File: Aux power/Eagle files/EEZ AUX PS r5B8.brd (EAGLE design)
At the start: 107 x 74 mm, 78 parts, among them IC1 LM25575, IC2 MC7812, IC3 TPD4E002DRLR, IC4 TPD2E001DZDR, IC5 ADUM3160BRWZ, Q1 BTA26-600, Q2 BTA26-600, Q3 IRLL014N, X1 282836-5, X2 09185067324, X3 22-23-2031, X4 LMJ2138812S0LOT6C, X5 826629-8, X6 826629-5, X7 SSW-105-02-S-S, X8 2411-01

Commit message: Rt value corrections for AUX PS and Power board
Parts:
- R11: value 30K -> 18K
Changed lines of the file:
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@@
 <text x="15.6845" y="37.9476" size="1.016" layer="125" ratio="10" rot="R180">SAR1</text>
 <text x="42.1505125" y="57.57349375" size="2.1844" layer="125" ratio="10" rot="SR0">TR1</text>
-<text x="13.035509375" y="57.16549375" size="1.27" layer="125" ratio="10">VAR1</text>
-<text x="17.861509375" y="57.16549375" size="1.27" layer="125" ratio="10">VAR2</text>
+<text x="12.845009375" y="57.16549375" size="1.27" layer="125" ratio="10">VAR1</text>
+<text x="17.925009375" y="57.16549375" size="1.27" layer="125" ratio="10">VAR2</text>
 <text x="1.613003125" y="61.6315" size="1.27" layer="125" ratio="10">X1</text>
 <text x="103.981503125" y="67.197503125" size="1.27" layer="125" ratio="10">X2</text>
@@
 <attribute name="VALUE" x="82.169" y="28.2575" size="1.016" layer="27" ratio="10"/>
 </element>
-<element name="R11" library="rcl" package="R0805" value="30K" x="82.2325" y="26.7335" smashed="yes">
+<element name="R11" library="rcl" package="R0805" value="18K" x="82.2325" y="26.7335" smashed="yes">
 <attribute name="NAME" x="81.1149" y="24.5364" size="1.016" layer="25" ratio="10"/>
 <attribute name="VALUE" x="84.0486" y="27.1399" size="0.9906" layer="27" ratio="10" rot="R180"/>
@@
 <element name="C8" library="rcl" package="C0805" value="100n" x="79.3115" y="36.957" smashed="yes" rot="R180">
 <attribute name="NAME" x="81.407" y="37.6555" size="1.016" layer="25" ratio="10" rot="SR270"/>
-<attribute name="VALUE" x="81.534" y="37.4015" size="1.27" layer="27" rot="R180"/>
+<attribute name="VALUE" x="77.597" y="36.449" size="1.016" layer="27" ratio="10"/>
 </element>
 <element name="C7" library="rcl" package="C0805" value="22n" x="85.217" y="28.0035" smashed="yes" rot="R270">
@@
 <element name="R7" library="rcl" package="R0805" value="15K" x="71.9455" y="36.83" smashed="yes" rot="R270">
 <attribute name="NAME" x="69.7865" y="37.5285" size="1.016" layer="25" ratio="10" rot="SR270"/>
-<attribute name="VALUE" x="71.3105" y="38.354" size="1.27" layer="27" rot="R270"/>
+<attribute name="VALUE" x="71.374" y="38.227" size="1.016" layer="27" ratio="10" rot="R270"/>
 </element>
 <element name="R8" library="rcl" package="R0805" value="2K2" x="71.9455" y="40.767" smashed="yes" rot="R270">
 <attribute name="NAME" x="71.1835" y="42.926" size="1.016" layer="25" ratio="10"/>
-<attribute name="VALUE" x="72.4535" y="39.1795" size="1.27" layer="27" rot="R90"/>
+<attribute name="VALUE" x="72.4535" y="39.497" size="1.016" layer="27" ratio="10" rot="R90"/>
 </element>
 <element name="C9" library="rcl" package="C1210" value="4u7" x="71.501" y="47.625" smashed="yes" rot="R180">
@@
 <element name="X1" library="EEZ_Lib1" package="TBLOCK5.0_5" value="282836-5" x="4.4625" y="58.155" smashed="yes">
 <attribute name="NAME" x="1.613" y="61.6315" size="1.27" layer="25" ratio="10"/>
-<attribute name="VALUE" x="0.1525" y="33.265" size="1.27" layer="27"/>
+<attribute name="VALUE" x="1.66" y="43.7135" size="1.27" layer="27" rot="R90"/>
 </element>
 <element name="ZD2" library="EEZ_Lib1" package="DO201-BIDIR" value="1.5KE400CA" x="12.5355" y="23.737" smashed="yes">
@@
 <element name="L1" library="EEZ_Lib1" package="L1210" value="2u2" x="72.009" y="32.766" smashed="yes">
 <attribute name="NAME" x="68.2625" y="33.5915" size="1.27" layer="25" ratio="10" rot="SR270"/>
-<attribute name="VALUE" x="71.4375" y="34.417" size="1.27" layer="27" rot="R270"/>
+<attribute name="VALUE" x="70.358" y="32.131" size="1.27" layer="27"/>
 </element>
 <element name="Q1" library="triac" package="TOP3S-1" value="BTA26-600" x="46.0375" y="13.0175" smashed="yes" rot="R180">

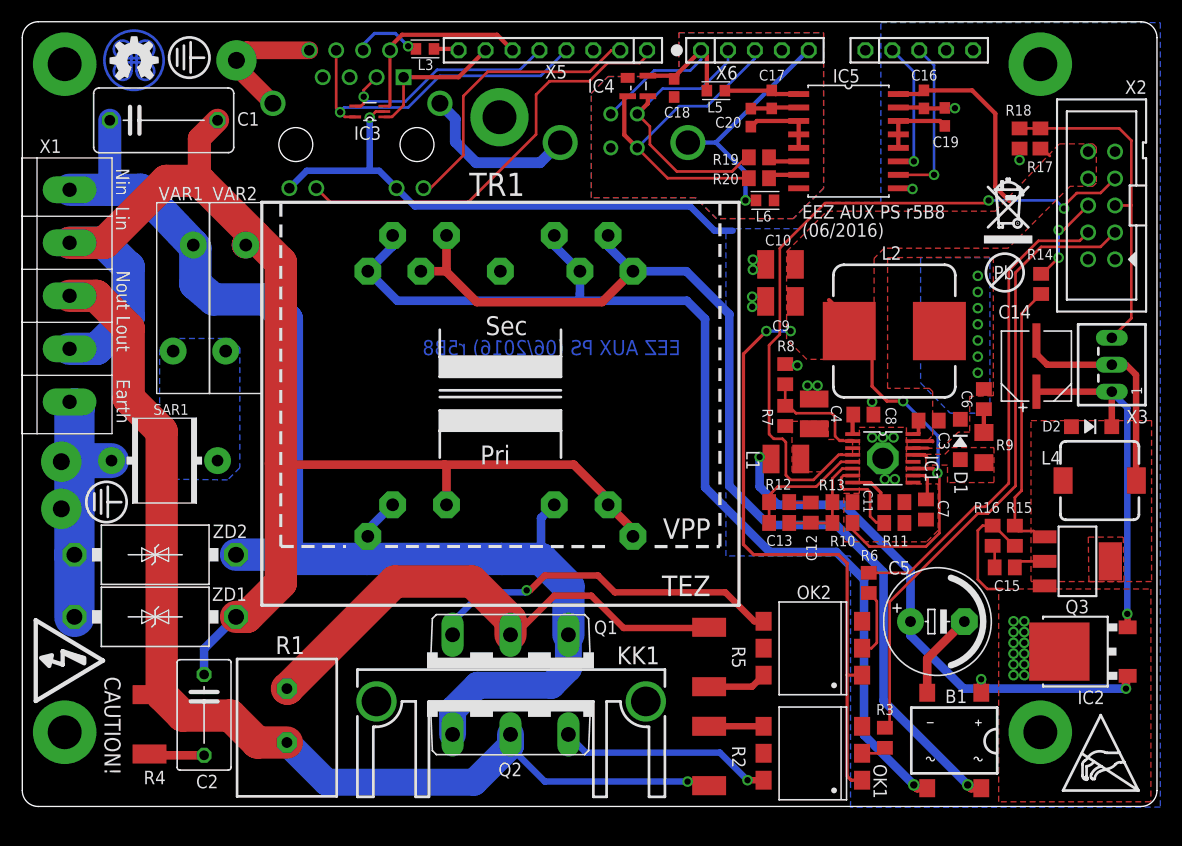
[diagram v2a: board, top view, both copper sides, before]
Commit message: AUX PS renumbering
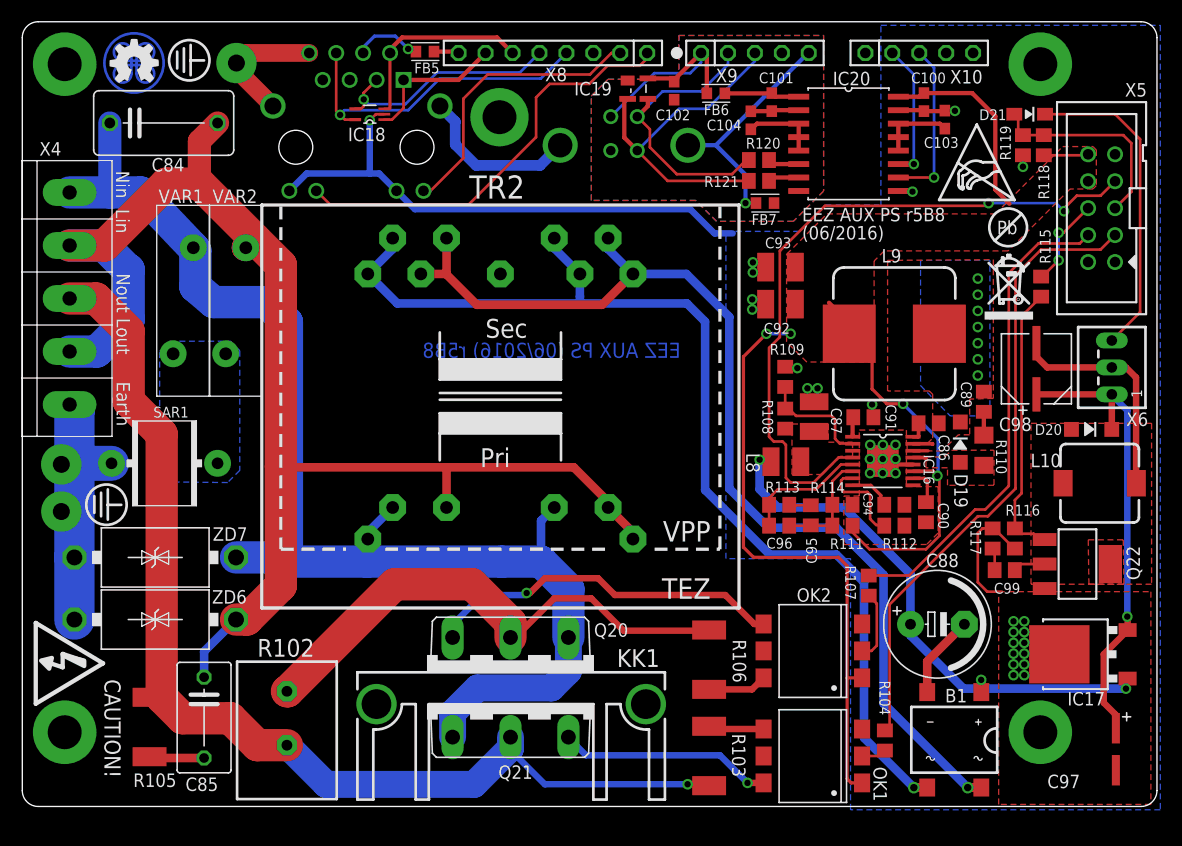
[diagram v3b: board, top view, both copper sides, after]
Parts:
- removed C1: 6n8 (X1), rcl:C102-064X133
- removed C10, C4, C9: 4u7, rcl:C1210
- removed C11: 1n, rcl:C0805
- removed C12: 3n9, rcl:C0805
- removed C13: 180p, rcl:C0805
- removed C14: 100u, EEZ_Lib1:CAPAE660X610N
- removed C15: 47n, rcl:C0805
- removed C16, C17, C18, C19, C20: 100n, rcl:C0603
- removed C2: 47n/400V, rcl:C075-052X106
- removed C3, C7: 22n, rcl:C0805
- removed C5: 1mF/25V, EEZ_Lib1:ECAP5/10.5
- removed C6: 330p, rcl:C0805
- removed C8: 100n, rcl:C0805
- removed D1: DFLS1100-7, EEZ_Lib1:SOD123
- removed D2: SKL16, EEZ_Lib1:SOD123
- removed EEZ_SIGNATURE: SIGNATURESMALL, EEZ_Lib1:SIGNATURE_5MM
- removed IC1: LM25575, EEZ_Lib1:SOP65P640X110-17N_HOLE
- removed IC2: MC7812, EEZ_Lib1:TO252
- removed IC3: TPD4E002DRLR, EEZ_Lib1:SOT50P280X60-5N
- removed IC4: TPD2E001DZDR, EEZ_Lib1:SOP192P292X122-4N
- removed IC5: ADUM3160BRWZ, MyLib6:SOIC-16W
- removed L1: 2u2, EEZ_Lib1:L1210
- removed L2: 100uH (MSS1260-104K), EEZ_Lib1:MSS1278
- removed L3: 60R@100MHz, MyLib6:BEAD0603
- removed L4: 470u, EEZ_Lib1:DE0704
- removed L5, L6: 2506033007Y3, MyLib6:BEAD0603
- removed Q1, Q2: BTA26-600, triac:TOP3S-1
- removed Q3: IRLL014N, transistor-power:SOT223
- removed R1: 15R/7W, EEZ_Lib1:R_0913
- removed R10: 5K6 1%, rcl:R0805
- removed R11: 18K, rcl:R0805
- removed R12: 20K, rcl:R0805
- removed R13: 1K8 1%, rcl:R0805
- removed R14: 100R, rcl:R0805
- removed R15: 47K, rcl:R0805
- removed R16: 1K, rcl:R0805
- removed R17: 5K6, rcl:R0805
- removed R18: 10K, rcl:R0805
- removed R19, R20: 22R, rcl:R0805
- removed R3, R6: 270R, rcl:R0805
- removed R4: 150R/2W, rcl:R2512
- removed R5: 330R/2W, rcl:R2512
- removed R7: 15K, rcl:R0805
- removed R8: 2K2, rcl:R0805
- removed R9: 10R, rcl:R1206
- removed TR1: TEZ6/D230/15V, EEZ_Lib1:PCB_TRAFO6VA_TEZ+VPP
- removed U$2: (no value), olimex_logo1:RECYCLE_BIN1/8
- removed U$3: (no value), olimex_logo1:PB_SMALL
- removed U$4: (no value), olimex_logo1:ESD_SYMBOL
- removed X1: 282836-5, EEZ_Lib1:TBLOCK5.0_5
- removed X2: 09185067324, EEZ_Lib1:IDC-10PIN
- removed X3: 22-23-2031, con-molex:22-23-2031
- removed ZD1, ZD2: 1.5KE400CA, EEZ_Lib1:DO201-BIDIR
- added C100, C101, C102, C103, C104: 100n, rcl:C0603
- added C84: 6n8 (X1), rcl:C102-064X133
- added C85: 47n/400V, rcl:C075-052X106
- added C86, C90: 22n, rcl:C0805
- added C87, C92, C93: 4u7, rcl:C1210
- added C88: 1mF/25V, EEZ_Lib1:ECAP5/10.5
- added C89: 330p, rcl:C0805
- added C91: 100n, rcl:C0805
- added C94: 1n, rcl:C0805
- added C95: 3n9, rcl:C0805
- added C96: 180p, rcl:C0805
- added C97: 10u, MyLib6:PANASONIC_C
- added C98: 100u, EEZ_Lib1:CAPAE660X610N
- added C99: 47n, rcl:C0805
- added D19: DFLS1100-7, EEZ_Lib1:SOD123
- added D20: SKL16, EEZ_Lib1:SOD123
- added D21: BAS316, diode:SOD323-W
- added EEZ_SIGNATURE1: SIGNATURESMALL, EEZ_Lib1:SIGNATURE_5MM
- added FB5, FB6, FB7: 60R@100MHz, MyLib6:BEAD0603
- added IC16: LM25575, EEZ_Lib1:SOP65P640X110-17N
- added IC17: MC7812, EEZ_Lib1:TO252
- added IC18: TPD4E002DRLR, EEZ_Lib1:SOT50P280X60-5N
- added IC19: TPD2E001DZDR, EEZ_Lib1:SOP192P292X122-4N
- added IC20: ADUM3160BRWZ, MyLib6:SOIC-16W
- added L10: 470u, EEZ_Lib1:DE0704
- added L8: 2u2, EEZ_Lib1:L1210
- added L9: 100uH (MSS1260-104K), EEZ_Lib1:MSS1278
- added Q20, Q21: BTA26-600, triac:TOP3S-1
- added Q22: IRLL014N, transistor-power:SOT223
- added R102: 15R/7W, EEZ_Lib1:R_0913
- added R104, R107: 270R, rcl:R0805
- added R105: 150R/2W, rcl:R2512
- added R106: 330R/2W, rcl:R2512
- added R108: 15K, rcl:R0805
- added R109: 2K2, rcl:R0805
- added R110: 10R, rcl:R1206
- added R111: 5K6 1%, rcl:R0805
- added R112: 18K, rcl:R0805
- added R113: 20K, rcl:R0805
- added R114: 1K8 1%, rcl:R0805
- added R115: 100R, rcl:R0805
- added R116: 47K, rcl:R0805
- added R117: 1K, rcl:R0805
- added R118: 5K6, rcl:R0805
- added R119: 10K, rcl:R0805
- added R120, R121: 22R, rcl:R0805
- added TR2: TEZ6/D230/12V, EEZ_Lib1:PCB_TRAFO6VA_TEZ+VPP
- added U$1: (no value), olimex_logo1:RECYCLE_BIN1/8
- added U$5: (no value), olimex_logo1:PB_SMALL
- added U$6: (no value), olimex_logo1:ESD_SYMBOL
- added X10, X9: 826629-5, con-samtec:SSW-105-02-S-S
- added X11: 2411-01, con-kycon:KUSBVX-BS1N
- added ZD6, ZD7: 1.5KE400CA, EEZ_Lib1:DO201-BIDIR
- X4: value LMJ2138812S0LOT6C -> 282836-5; device EEZ_Lib1:RJ45-VERT -> EEZ_Lib1:TBLOCK5.0_5
- X5: value 826629-8 -> 09185067324; device con-samtec:SSW-108-02-S-S -> EEZ_Lib1:IDC-10PIN
- X6: value 826629-5 -> 22-23-2031; device con-samtec:SSW-105-02-S-S -> con-molex:22-23-2031
- X7: value SSW-105-02-S-S -> LMJ2138812S0LOT6C; device con-samtec:SSW-105-02-S-S -> EEZ_Lib1:RJ45-VERT
- X8: value 2411-01 -> 826629-8; device con-kycon:KUSBVX-BS1N -> con-samtec:SSW-108-02-S-S
- moved X5 53.8 mm to (101.8, 56.4), turned to 90 degrees
- moved X7 53.7 mm to (31.5, 63.4), flipped to the bottom, turned to 180 degrees
- moved X6 45.0 mm to (102.7, 41.4), turned to 90 degrees
- moved X4 27.7 mm to (4.46, 57.9), flipped to the top, turned to 0 degrees
- moved X8 10.8 mm to (50.0, 71.1), flipped to the top, turned to 180 degrees
- moved VAR1 0.25 mm to (15.2, 47.7)
- moved VAR2 0.25 mm to (20.1, 47.7)
- moved KK1 0.25 mm to (46.1, 9.65)
- moved OK1 0.25 mm to (74.5, 4.76)
- moved OK2 0.25 mm to (74.5, 14.7)
- moved SAR1 0.25 mm to (18.4, 32.4)
- moved B1 0.06 mm to (87.9, 6.29)
- renumbered R2 to R103
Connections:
- removed net +3V3: L3.P$2, X5.8
- removed net AC_IN1: C1.1, Q1.A1, Q2.A1, TR1.P1.2V, TR1.P2.2V, TR1.P2_TEZ, VAR1.P$2, X1.1, ZD2.A
- removed net AC_IN2: C1.2, C2.1, TR1.P1.1V, TR1.P1_TEZ, TR1.P2.1V, VAR2.P$1, X1.2, X1.4, ZD1.A
- removed net DC_PREG1: C4.1, IC1.3, L1.2, R7.2
- removed net ETH_ACTLED: X4.YA, X5.2
- removed net ETH_IN+: IC3.5, X4.6, X5.4
- removed net ETH_IN-: IC3.4, X4.3, X5.5
- removed net ETH_LINKLED: X4.GA, X5.1
- removed net ETH_OUT+: IC3.3, X4.2, X5.6
- removed net ETH_OUT-: IC3.1, X4.1, X5.7
- removed net FAN_CONTROL: R14.2, X2.6
- removed net FAN_SENSE: R17.2, R18.1, X2.5, X3.3
- removed net IS: D1.A, IC1.13, R9.1
- removed net N$1: C6.2, R9.2
- removed net N$10: Q1.A2, R1.1, R5.2
- removed net N$11: Q2.A2, R1.2, R103.2, R4.1, X1.3
- removed net N$12: C15.1, R16.2
- removed net N$128: C12.1, C13.1, IC1.6, R10.2, R13.1
- removed net N$13: IC1.4, X2.7
- removed net N$131: C3.2, IC1.16
- removed net N$135: C13.2, IC1.5, R12.1
- removed net N$165: IC1.7, R11.1
- removed net N$166: C8.2, IC1.1
- removed net N$167: C11.2, IC1.8
- removed net N$168: C7.1, IC1.10
- removed net N$17: Q3.1, R14.1, R15.2
- removed net N$180: IC1.2, R7.1, R8.2
- removed net N$2: OK1.6, Q2.G
- removed net N$20: B1.AC2, TR1.S1.2T, TR1.S1.2V, TR1.S2.2T, TR1.S2.2V
- removed net N$21: C14.2, L4.1, X3.2
- removed net N$4: OK2.4, Q1.G
- removed net N$5: OK1.2, R3.1
- removed net N$50: C20.1, IC5.3, IC5.4, IC5.5
- removed net N$53: IC5.7, R20.2
- removed net N$54: C17.1, IC5.1, L5.P$2
- removed net N$6: OK2.2, R6.1
- removed net N$7: OK2.6, R5.1
- removed net N$77: C12.2, R12.2
- removed net N$8: C2.2, R4.2
- removed net N$9: B1.AC1, TR1.S1.1T, TR1.S1.1V, TR1.S2.1T, TR1.S2.1V
- removed net PWR_DIRECT: R3.2, X2.3
- removed net PWR_SSTART: R6.2, X2.4
- removed net SW: C3.1, C6.1, D1.C, IC1.14, IC1.15, L2.1
- new net AC_IN1_MAIN: C84.1, Q20.A1, Q21.A1, TR2.P1.2V, TR2.P2.2V, TR2.P2_TEZ, VAR1.P$2, X4.1, ZD7.A
- new net AC_IN2_MAIN: C84.2, C85.1, TR2.P1.1V, TR2.P1_TEZ, TR2.P2.1V, VAR2.P$1, X4.2, X4.4, ZD6.A
- new net AUX_+3V3: FB5.P$2, X8.8
- new net AUX_ETH_ACTLED: X7.YA, X8.2
- new net AUX_ETH_IN+: IC18.5, X7.6, X8.4
- new net AUX_ETH_IN-: IC18.4, X7.3, X8.5
- new net AUX_ETH_LINKLED: X7.GA, X8.1
- new net AUX_ETH_OUT+: IC18.3, X7.2, X8.6
- new net AUX_ETH_OUT-: IC18.1, X7.1, X8.7
- new net AUX_FAN_CTRL: R115.2, X5.6
- new net AUX_FAN_SENSE: D21.A, R118.2, R119.1, X5.5
- new net AUX_PWR_DIRECT: R104.2, X5.3
- new net AUX_PWR_SSTART: R107.2, X5.4
- new net DC_PREG2: C87.1, IC16.3, L8.2, R108.2
- new net IS1: D19.A, IC16.13, R110.1
- new net N$163: D21.C, X6.3
- new net N$58: C86.2, IC16.16
- new net N$59: C96.2, IC16.5, R113.1
- new net N$60: IC16.7, R112.1
- new net N$61: C91.2, IC16.1
- new net N$63: C94.2, IC16.8
- new net N$66: C90.1, IC16.10
- new net N$68: IC16.4, X5.7
- new net N$69: IC16.2, R108.1, R109.2
- new net N$70: C89.2, R110.2
- new net N$71: OK1.6, Q21.G
- new net N$72: OK2.4, Q20.G
- new net N$73: OK2.6, R106.1
- new net N$74: OK1.2, R104.1
- new net N$75: OK2.2, R107.1
- new net N$78: B1.AC1, TR2.S1.1T, TR2.S1.1V, TR2.S2.1T, TR2.S2.1V
- new net N$80: B1.AC2, TR2.S1.2T, TR2.S1.2V, TR2.S2.2T, TR2.S2.2V
- new net N$81: Q20.A2, R102.1, R106.2
- new net N$82: Q21.A2, R102.2, R103.2, R105.1, X4.3
- new net N$83: C85.2, R105.2
- new net N$84: C99.1, R117.2
- new net N$85: Q22.1, R115.1, R116.2
- new net N$86: C98.2, L10.1, X6.2
- new net N$87: C104.1, IC20.3, IC20.4, IC20.5
- new net N$88: IC20.6, R120.2
- new net N$89: IC20.7, R121.2
- new net N$90: C101.1, FB6.P$2, IC20.1
- new net N$91: C103.1, IC20.12, IC20.13, IC20.14
- new net SW2: C86.1, C89.1, D19.C, IC16.14, IC16.15, L9.1
- net +5V: now also C100.1, C92.1, C93.1, IC16.11, IC20.16, L9.2, R111.1, R118.1, X5.10, X5.8; no longer C10.1, C16.1, C9.1, IC1.11, IC5.16, L2.2, R10.1, R17.1, X2.10, X2.8
- net 12VDC: now also C97.1, C98.1, D20.C, IC17.2, X6.1; no longer C14.1, D2.C, IC2.2, X3.1
- net AC_EARTH: now also FB7.P$1, X11.M1, X11.M2, X4.5, X7.8, X7.SH1, X7.SH2, X9.5, ZD6.C, ZD7.C; no longer L6.P$1, X1.5, X4.8, X4.SH1, X4.SH2, X6.5, X8.M1, X8.M2, ZD1.C, ZD2.C
- net D+: now also IC19.2, R121.1, X11.3, X9.3; no longer IC4.2, R20.1, X6.3, X8.3
- net D-: now also IC19.3, R120.1, X11.2, X9.2; no longer IC4.3, R19.1, X6.2, X8.2
- net FAN_OUT: now also C99.2, D20.A, L10.2, Q22.2, Q22.4; no longer C15.2, D2.A, L4.2, Q3.2, Q3.4
- net GND: now also C100.2, C103.2, C87.2, C88.-, C90.2, C91.1, C92.2, C93.2, C94.1, C97.2, IC16.12, IC16.9, IC16.TP, IC17.3, IC18.2, IC20.15, IC20.9, Q22.3, R109.1, R112.2, R114.2, R116.1, R117.1, R119.2, X5.1, X5.2, X5.9, X7.GC, X7.YC; no longer C10.2, C11.1, C16.2, C19.2, C4.2, C5.-, C7.2, C8.1, C9.2, IC1.12, IC1.9, IC1.TP, IC1.TP2, IC2.3, IC3.2, IC5.15, IC5.9, Q3.3, R11.2, R13.2, R15.1, R16.1, R18.2, R8.1, X2.1, X2.2, X2.9, X4.GC, X4.YC
- net MCU_D+: now also IC20.10, X10.3; no longer IC5.10, X7.3
- net MCU_D-: now also IC20.11, X10.2; no longer IC5.11, X7.2
- net N$125: now also FB5.P$1, X7.4; no longer L3.P$1, X4.4
- net N$52: now also C95.2, R113.2; no longer IC5.6, R19.2
- net N$57: now also C95.1, C96.1, IC16.6, R111.2, R114.1; no longer C19.1, IC5.12, IC5.13, IC5.14
- net VIN: now also C88.+, IC17.1, L8.1; no longer C5.+, IC2.1, L1.1
- net XUSB_GND: now also C101.2, C102.1, C104.2, FB7.P$2, IC19.1, IC20.2, IC20.8, X11.4, X9.4; no longer C17.2, C18.1, C20.2, IC4.1, IC5.2, IC5.8, L6.P$2, X6.4, X8.4
- net XUSB_VBUS: now also C102.2, FB6.P$1, IC19.4, X11.1, X9.1; no longer C18.2, IC4.4, L5.P$1, X6.1, X8.1
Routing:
- net AC_IN2_MAIN: track 0.00 -> 134.3 mm
- net AC_IN2: track 134.3 -> 0.00 mm
- net AC_IN1_MAIN: track 0.00 -> 125.9 mm
- net AC_IN1: track 125.9 -> 0.00 mm
- net N$11: track 103.0 -> 0.00 mm, vias 1 -> 0
- net N$82: track 0.00 -> 102.8 mm, vias 0 -> 1
- net N$20: track 102.3 -> 0.00 mm, vias 1 -> 0
- net N$80: track 0.00 -> 102.2 mm, vias 0 -> 1
- net N$9: track 99.8 -> 0.00 mm, vias 1 -> 0
- net N$78: track 0.00 -> 99.7 mm, vias 0 -> 1
- net N$68: track 0.00 -> 65.5 mm, vias 0 -> 2
- net N$13: track 65.5 -> 0.00 mm, vias 2 -> 0
- net PWR_DIRECT: track 59.5 -> 0.00 mm
- net AUX_PWR_DIRECT: track 0.00 -> 59.5 mm
- net N$81: track 0.00 -> 49.7 mm
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- added copper zone on layer 1, net DC_PREG2
- added copper zone on layer 1, net IS1
- added copper zone on layer 1, net SW2
- added copper zone on layer 16, net SW2
- removed copper zone on layer 1, net DC_PREG1
- removed copper zone on layer 1, net IS
- removed copper zone on layer 1, net SW
- removed copper zone on layer 16, net SW
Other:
- board text added: "C100"
- board text added: "C101"
- board text added: "C102"
- board text added: "C103"
- board text added: "C104"
- board text added: "C84"
- board text added: "C85"
- board text added: "C86"
- board text added: "C87"
- board text added: "C88"
- board text added: "C89"
- board text added: "C90"
- board text added: "C91"
- board text added: "C92"
- board text added: "C93"
- board text added: "C94"
- board text added: "C95"
- board text added: "C96"
- board text added: "C97"
- board text added: "C98"
- board text added: "C99"
- board text added: "D19"
- board text added: "D20"
- board text added: "D21"
- board text added: "FB5"
- board text added: "FB6"
- board text added: "FB7"
- board text added: "Fan X6"
- board text added: "Fan sense (Yellow) 3"
- board text added: "Fan+ (Red) 1"
- board text added: "Fan- (Black) 2"
- board text added: "IC16"
- board text added: "IC17"
- board text added: "IC18"
- board text added: "IC19"
- board text added: "IC20"
- board text added: "L10"
- board text added: "L8"
- board text added: "L9"
- board text added: "Power X5"
- board text added: "Q20"
- board text added: "Q21"
- board text added: "Q22"
- board text added: "R102"
- board text added: "R103"
- board text added: "R104"
- board text added: "R105"
- board text added: "R106"
- board text added: "R107"
- board text added: "R108"
- board text added: "R109"
- board text added: "R110"
- board text added: "R111"
- board text added: "R112"
- board text added: "R113"
- board text added: "R114"
- board text added: "R115"
- board text added: "R116"
- board text added: "R117"
- board text added: "R118"
- board text added: "R119"
- board text added: "R120"
- board text added: "R121"
- board text added: "RJ-45 Ethernet X8"
- board text added: "TR2"
- board text added: "USB (non-isolated) X9"
- board text added: "X10"
- board text added: "X11"
- board text added: "X7"
- board text added: "X9"
- board text added: "ZD6"
- board text added: "ZD7"
- board text removed: "C1"
- board text removed: "C10"
- board text removed: "C11"
- board text removed: "C12"
- board text removed: "C13"
- board text removed: "C14"
- board text removed: "C15"
- board text removed: "C16"
- board text removed: "C17"
- board text removed: "C18"
- board text removed: "C19"
- board text removed: "C2"
- board text removed: "C20"
- board text removed: "C3"
- board text removed: "C4"
- board text removed: "C5"
- board text removed: "C6"
- board text removed: "C7"
- board text removed: "C8"
- board text removed: "C9"
- board text removed: "D1"
- board text removed: "D2"
- board text removed: "IC1"
- board text removed: "IC2"
- board text removed: "IC3"
- board text removed: "IC4"
- board text removed: "IC5"
- board text removed: "L1"
- board text removed: "L2"
- board text removed: "L3"
- board text removed: "L4"
- board text removed: "L5"
- board text removed: "L6"
- board text removed: "Power X2"
- board text removed: "Q1"
- board text removed: "Q2"
- board text removed: "Q3"
- board text removed: "R1"
- board text removed: "R10"
- board text removed: "R11"
- board text removed: "R12"
- board text removed: "R13"
- board text removed: "R14"
- board text removed: "R15"
- board text removed: "R16"
- board text removed: "R17"
- board text removed: "R18"
- board text removed: "R19"
- board text removed: "R2"
- board text removed: "R20"
- board text removed: "R3"
- board text removed: "R4"
- board text removed: "R5"
- board text removed: "R6"
- board text removed: "R7"
- board text removed: "R8"
- board text removed: "R9"
- board text removed: "RJ-45 Ethernet X5"
- board text removed: "TR1"
- board text removed: "USB (non-isolated) X6"
- board text removed: "X1"
- board text removed: "X2"
- board text removed: "X3"
- board text removed: "ZD1"
- board text removed: "ZD2"

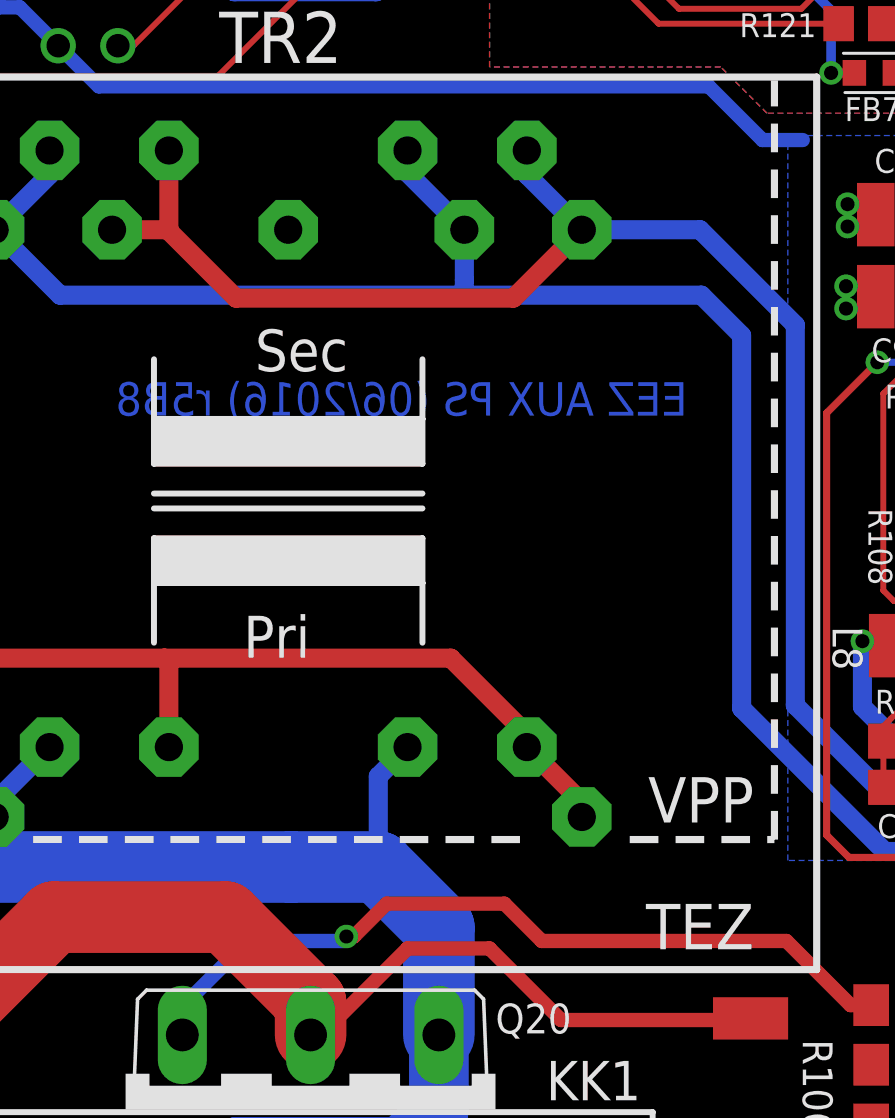
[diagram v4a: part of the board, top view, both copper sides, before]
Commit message: Myrra AC/DC module for 115VAC, BOM updated
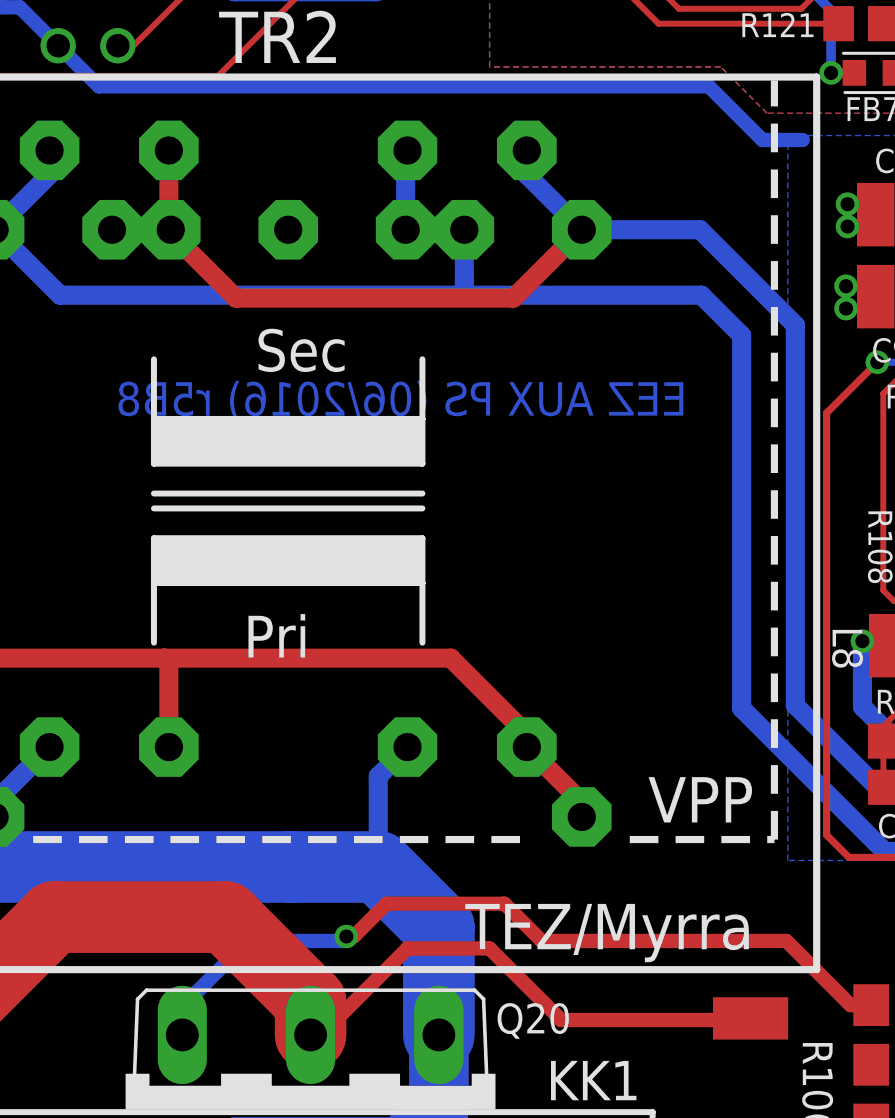
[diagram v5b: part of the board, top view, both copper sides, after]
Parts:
- TR2: device EEZ_Lib1:PCB_TRAFO6VA_TEZ+VPP -> EEZ_Lib1:PCB_TRAFO6VA_7.5W
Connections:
- net N$78: now also TR2.S2M
- net N$80: now also TR2.S1M
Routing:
- net N$80: track 102.2 -> 103.8 mm
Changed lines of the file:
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@@
 <layer number="27" name="tValues" color="10" fill="1" visible="no" active="yes"/>
 <layer number="28" name="bValues" color="11" fill="1" visible="no" active="yes"/>
-<layer number="29" name="tStop" color="7" fill="3" visible="yes" active="yes"/>
+<layer number="29" name="tStop" color="7" fill="3" visible="no" active="yes"/>
 <layer number="30" name="bStop" color="7" fill="6" visible="no" active="yes"/>
 <layer number="31" name="tCream" color="7" fill="4" visible="no" active="yes"/>
@@
 <layer number="37" name="tTest" color="7" fill="1" visible="no" active="yes"/>
 <layer number="38" name="bTest" color="7" fill="1" visible="no" active="yes"/>
-<layer number="39" name="tKeepout" color="15" fill="1" visible="yes" active="yes"/>
+<layer number="39" name="tKeepout" color="15" fill="1" visible="no" active="yes"/>
 <layer number="40" name="bKeepout" color="13" fill="1" visible="no" active="yes"/>
 <layer number="41" name="tRestrict" color="4" fill="10" visible="no" active="yes"/>
@@
 <element name="U$5" library="olimex_logo1" package="PB_SMALL" value="" x="92.9685" y="54.611" smashed="yes"/>
 <element name="U$6" library="olimex_logo1" package="ESD_SYMBOL" value="" x="86.456" y="57.1925" smashed="yes"/>
-<element name="TR2" library="EEZ_Lib1" package="PCB_TRAFO6VA_TEZ+VPP" value="TEZ6/D230/12V" x="45.085" y="37.719" smashed="yes" rot="R270">
-<attribute name="TME" value="TEZ6/D/15-15V" x="45.085" y="37.719" size="1.778" layer="27" rot="R270" display="off"/>
-<attribute name="MOUSER" value="553-VPP28-180" x="45.085" y="37.719" size="1.778" layer="27" rot="R270" display="off"/>
-<attribute name="NEWARK" value="37B9209" x="45.085" y="37.719" size="1.778" layer="27" rot="R270" display="off"/>
-<attribute name="DIGIKEY" value="237-1086-ND" x="45.085" y="37.719" size="1.778" layer="27" rot="R270" display="off"/>
+<element name="TR2" library="EEZ_Lib1" package="PCB_TRAFO6VA_7.5W" value="TEZ6/D230/12V" x="45.085" y="37.719" smashed="yes" rot="R270">
 <attribute name="NAME" x="42.1505" y="57.3195" size="2.1844" layer="25" ratio="10" rot="SR0"/>
 <attribute name="VALUE" x="33.324" y="36.7455" size="2.1844" layer="27" ratio="10"/>
@@
 <wire x1="89.7805" y1="1.7865" x2="89.154" y2="1.778" width="0.8128" layer="1"/>
 <wire x1="81.2165" y1="9.7155" x2="89.154" y2="1.778" width="0.8128" layer="16"/>
+<contactref element="TR2" pad="S2M"/>
+<wire x1="40.005" y1="50.2825" x2="40.085" y2="50.219" width="0" layer="19" extent="1-1"/>
 </signal>
 <signal name="N$80">
@@
 <wire x1="34.925" y1="53.594" x2="34.925" y2="52.559" width="0.8128" layer="16"/>
 <wire x1="34.925" y1="52.559" x2="32.585" y2="50.219" width="0.8128" layer="16"/>
-<wire x1="50.165" y1="53.594" x2="50.165" y2="52.639" width="0.8128" layer="16"/>
-<wire x1="50.165" y1="52.639" x2="52.585" y2="50.219" width="0.8128" layer="16"/>
 <wire x1="52.585" y1="50.219" x2="52.585" y2="48.0765" width="0.8128" layer="16"/>
 <wire x1="52.585" y1="48.0765" x2="52.578" y2="47.4345" width="0.8128" layer="16"/>
@@
 <wire x1="84.51" y1="1.7865" x2="84.074" y2="1.778" width="0.8128" layer="1"/>
 <wire x1="79.375" y1="6.477" x2="84.074" y2="1.778" width="0.8128" layer="16"/>
+<contactref element="TR2" pad="S1M"/>
+<wire x1="52.585" y1="50.219" x2="50.085" y2="50.219" width="0.8128" layer="16"/>
+<wire x1="50.165" y1="53.594" x2="50.085" y2="53.594" width="0.8128" layer="16"/>
+<wire x1="50.085" y1="53.594" x2="50.085" y2="50.219" width="0.8128" layer="16"/>
 </signal>
 <signal name="TA5">
